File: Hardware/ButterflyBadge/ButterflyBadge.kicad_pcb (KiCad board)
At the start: 2 copper layers, 18 x 65 mm, 614 parts, among them J1 USB_C_Receptacle_USB2.0, M1 Motor_DC, P1 TC2030-CTX, Q1 ALS-PT19, SW1 SW_Push, SW3 SW_SPDT, U1 W25Q128JVS, U11 SN74LV1T34DBV, U12 SN74LV1T34DBV, U13 XC6206PxxxMR, U19 SN74LV1T34DBV, U2 CN3058, U20 SN74LV1T34DBV, U21 XC6206PxxxMR, U23 HX612, U25 AP3722AT, U3 RP2040, U4 AX5201, U5 AMS1117-3.3, U6 Si24R1, U7 TFDU4301, U8 SM351LT, U9 TMI8118, X1 Badgelife_sao_connector_v169b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, X2 Badgelife_sao_connector_v169b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, Y1 12MHz, Y2 16MHz

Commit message: More schematic and PCB work Bang
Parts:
- AE1, J1: moved to B.Cu
- BT1: footprint Battery:BatteryHolder_Keystone_1042_1x18650 -> Battery:BatteryHolder_Keystone_2460_1xAA; moved to B.Cu
- P1: footprint Resistor_SMD:R_0402_1005Metric -> Tag-Connect:TC2030-MCP-NL
- U4: footprint Package_SO:SOIC-8-1EP_3.9x4.9mm_P1.27mm_EP2.29x3mm_ThermalVias -> Package_SO:SOIC-8_3.9x4.9mm_P1.27mm
- moved R11 299.4 mm to (109.5, -104.0)
- moved R10 298.6 mm to (109.5, -105.0)
- moved R3 298.0 mm to (99.0, -79.5)
- moved P1 289.9 mm to (99.0, -82.0)
- moved R1 288.8 mm to (95.5, -71.5)
- moved C3 285.0 mm to (108.5, -69.4)
- moved C9 282.1 mm to (111.4, -73.3)
- moved C11 282.1 mm to (111.4, -69.4)
- moved SW1 281.4 mm to (89.0, -72.5)
- moved C10 280.9 mm to (111.4, -71.4)
- moved R17 280.0 mm to (155.0, -125.0), turned to 90 degrees
- moved R22 279.7 mm to (111.4, -65.5)
- moved C5 279.4 mm to (108.5, -65.5)
- moved R6 279.4 mm to (120.0, -83.0)
- moved R4 279.1 mm to (164.5, -127.0)
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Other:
- board size 18 x 65 mm -> 20 x 80.5 mm

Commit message: Hardware mods
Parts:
- removed AE1: Antenna, RF_Antenna:Texas_SWRA117D_2.4GHz_Left
- removed REF**: BatteryHolder_Keystone_2460_1xAA, Battery:BatteryHolder_Keystone_2460_1xAA
- added AE2: Antenna_Chip, Resistor_SMD:R_1206_3216Metric, F.Cu at (163.5, -83.8)
- C20: footprint Capacitor_SMD:C_0603_1608Metric -> Capacitor_SMD:C_0402_1005Metric
- moved C2 66.4 mm to (155.2, -103.0)
- moved Y1 66.4 mm to (155.2, -105.2)
- moved SW1 64.8 mm to (152.8, -84.2), turned to -90 degrees
- moved C4 62.7 mm to (156.5, -107.8), turned to 180 degrees
- moved R22 58.8 mm to (158.8, -100.2), turned to -90 degrees
- moved R1 58.6 mm to (151.2, -89.5)
- moved R3 57.7 mm to (152.0, -102.2), turned to 90 degrees
- moved C13 56.5 mm to (158.8, -98.2), turned to -90 degrees
- moved R7 55.3 mm to (158.8, -121.5), turned to -90 degrees
- moved P1 55.3 mm to (149.8, -104.0), turned to 90 degrees
- moved R6 53.9 mm to (157.8, -121.5), turned to -90 degrees
- moved C11 53.5 mm to (159.0, -93.8), turned to -90 degrees
- moved D518 52.3 mm to (158.0, -102.2), turned to 180 degrees
- moved C9 51.3 mm to (153.8, -102.2), turned to 90 degrees
- moved C5 50.5 mm to (151.8, -91.5), turned to 180 degrees
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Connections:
- net Net-(U3-USB_DM) renamed /USB_RES+
- net Net-(U3-USB_DP) renamed /USB_RES-
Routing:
- net unconnected-(AE2-PCB_Trace): track 0.00 -> 3.27 mm

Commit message: Almost had the PCB done, need to restart. Sad face
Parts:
- removed AE2: Antenna_Chip, Resistor_SMD:R_1206_3216Metric
- removed C35, C38: 22uF, Capacitor_SMD:C_1206_3216Metric
- removed C36, C39: 10uF, Capacitor_SMD:C_0603_1608Metric
- removed C37, C40: 1uF, Capacitor_SMD:C_0402_1005Metric
- removed D10, D100, D101, D102, D103, D104, D105, D106, D107, D108, D109, D11, D110, D111, D112, D113, D114, D115, D116, D117, D118, D119, D12, D120, D121, D122, D123, D124, D125, D126, D127, D128, D129, D13, D130, D131, D132, D133, D134, D135, D136, D137, D138, D139, D14, D140, D141, D142, D143, D144, D145, D146, D147, D148, D149, D15, D150, D151, D152, D153, D154, D155, D156, D157, D158, D159, D16, D160, D161, D162, D163, D164, D165, D166, D167, D168, D169, D17, D170, D171, D172, D173, D174, D175, D176, D177, D178, D179, D18, D180, D181, D182, D183, D184, D185, D186, D187, D188, D189, D19, D190, D191, D192, D193, D194, D195, D196, D197, D198, D199, D20, D200, D201, D202, D203, D204, D205, D206, D207, D208, D209, D21, D210, D211, D212, D213, D214, D215, D216, D217, D218, D219, D22, D220, D221, D222, D223, D224, D225, D226, D227, D228, D229, D23, D230, D231, D232, D233, D234, D235, D236, D237, D238, D239, D24, D240, D241, D242, D243, D244, D245, D246, D247, D248, D249, D25, D250, D251, D252, D253, D254, D255, D256, D257, D258, D259, D26, D260, D261, D262, D263, D264, D265, D266, D267, D268, D269, D27, D270, D271, D272, D273, D274, D275, D276, D277, D278, D279, D28, D280, D281, D282, D283, D284, D285, D286, D287, D288, D289, D29, D290, D291, D292, D293, D294, D295, D296, D297, D298, D299, D3, D30, D300, D301, D302, D303, D304, D305, D306, D307, D308, D309, D31, D310, D311, D312, D313, D314, D315, D316, D317, D318, D319, D32, D320, D321, D322, D323, D324, D325, D326, D327, D328, D329, D33, D330, D331, D332, D333, D334, D335, D336, D337, D338, D339, D34, D340, D341, D342, D343, D344, D345, D346, D347, D348, D349, D35, D350, D351, D352, D353, D354, D355, D356, D357, D358, D359, D36, D360, D361, D362, D363, D364, D365, D366, D367, D368, D369, D37, D370, D371, D372, D373, D374, D375, D376, D377, D378, D379, D38, D380, D381, D382, D383, D384, D385, D386, D387, D388, D389, D39, D390, D391, D392, D393, D394, D395, D396, D397, D398, D399, D4, D40, D400, D401, D402, D403, D404, D405, D406, D407, D408, D409, D41, D410, D411, D412, D413, D414, D415, D416, D417, D418, D419, D42, D420, D421, D422, D423, D424, D425, D426, D427, D428, D429, D43, D430, D431, D432, D433, D434, D435, D436, D437, D438, D439, D44, D440, D441, D442, D443, D444, D445, D446, D447, D448, D449, D45, D450, D451, D452, D453, D454, D455, D456, D457, D458, D459, D46, D460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: SK6812, XL3528RGBW:XL-3528RGBW
- removed U11, U12, U19, U20: SN74LV1T34DBV, Package_TO_SOT_SMD:SOT-23-5
- removed U13, U21: XC6206PxxxMR, Package_TO_SOT_SMD:SOT-23
- removed U16: ~, Package_SO:SOP-8_3.9x4.9mm_P1.27mm
- removed U23: HX612, Package_SO:SOP-16_3.9x9.9mm_P1.27mm
- removed X1, X2: Badgelife_sao_connector_v169bis, badgelife_sao_v169bis:Badgelife-SAOv169-BADGE-2x3
- added AE1: Antenna, RF_Antenna:Texas_SWRA117D_2.4GHz_Left, F.Cu at (40.8, 124.7)
- added BZ1: Buzzer, ButterflyBadge:Buzzer-GSC5025YA-12R4000, F.Cu at (38.6, 128.8)
- added J4: Conn_02x07_Odd_Even, ButterflyBadge:FlatFlexWingConnector-PCBSide, F.Cu at (30.2, 127.9)
- added Q2: Q_NMOS_GSD, Package_TO_SOT_SMD:SOT-23, F.Cu at (36.1, 134.2)
- added R23: 0, Resistor_SMD:R_0402_1005Metric, F.Cu at (40.0, 132.9)
- added R24: 10K, Resistor_SMD:R_0402_1005Metric, F.Cu at (40.0, 134.9)
- BT1: footprint Battery:BatteryHolder_Keystone_2460_1xAA -> Battery:BatteryHolder_MPD_BH-18650-PC2
- U4: footprint Package_SO:SOIC-8_3.9x4.9mm_P1.27mm -> Package_SO:SOIC-8-1EP_3.9x4.9mm_P1.27mm_EP2.41x3.3mm_ThermalVias
- moved C15 207.1 mm to (228.2, 81.0)
- moved C21 207.1 mm to (229.2, 89.3)
- moved C42 207.1 mm to (220.2, 84.0)
- moved C43 207.1 mm to (229.2, 86.3)
- moved D2 207.1 mm to (234.2, 89.8)
- moved L1 207.1 mm to (233.7, 95.3)
- moved R12 207.1 mm to (229.2, 85.3)
- moved R13 207.1 mm to (229.2, 84.3)
- moved R8 207.1 mm to (231.7, 81.3)
- moved R9 207.1 mm to (236.7, 80.3)
- moved U5 207.1 mm to (222.2, 78.8)
- moved C16 201.6 mm to (91.5, 125.5)
- moved SW3 201.2 mm to (197.8, 135.6)
- moved C29 198.9 mm to (122.0, 127.4)
- moved C30 198.9 mm to (118.5, 132.4)
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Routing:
- net unconnected-(AE2-PCB_Trace): track 3.27 -> 0.00 mm
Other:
- board size 20 x 80.5 mm -> 26.7 x 96.5 mm

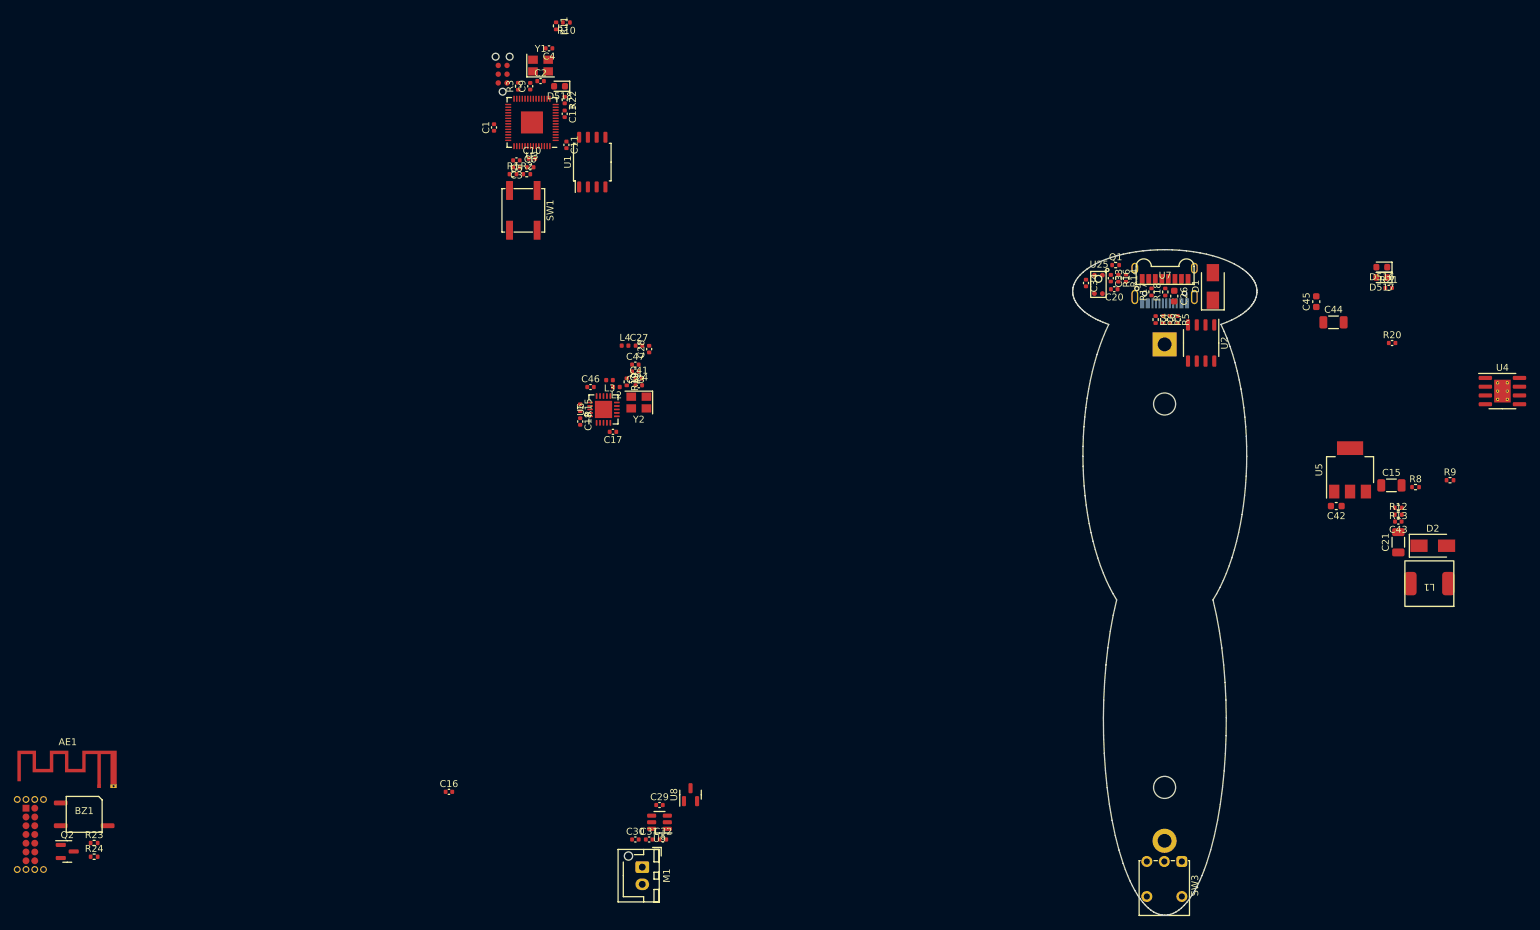
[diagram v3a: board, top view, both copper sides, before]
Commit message: Component placement is done, now for layout
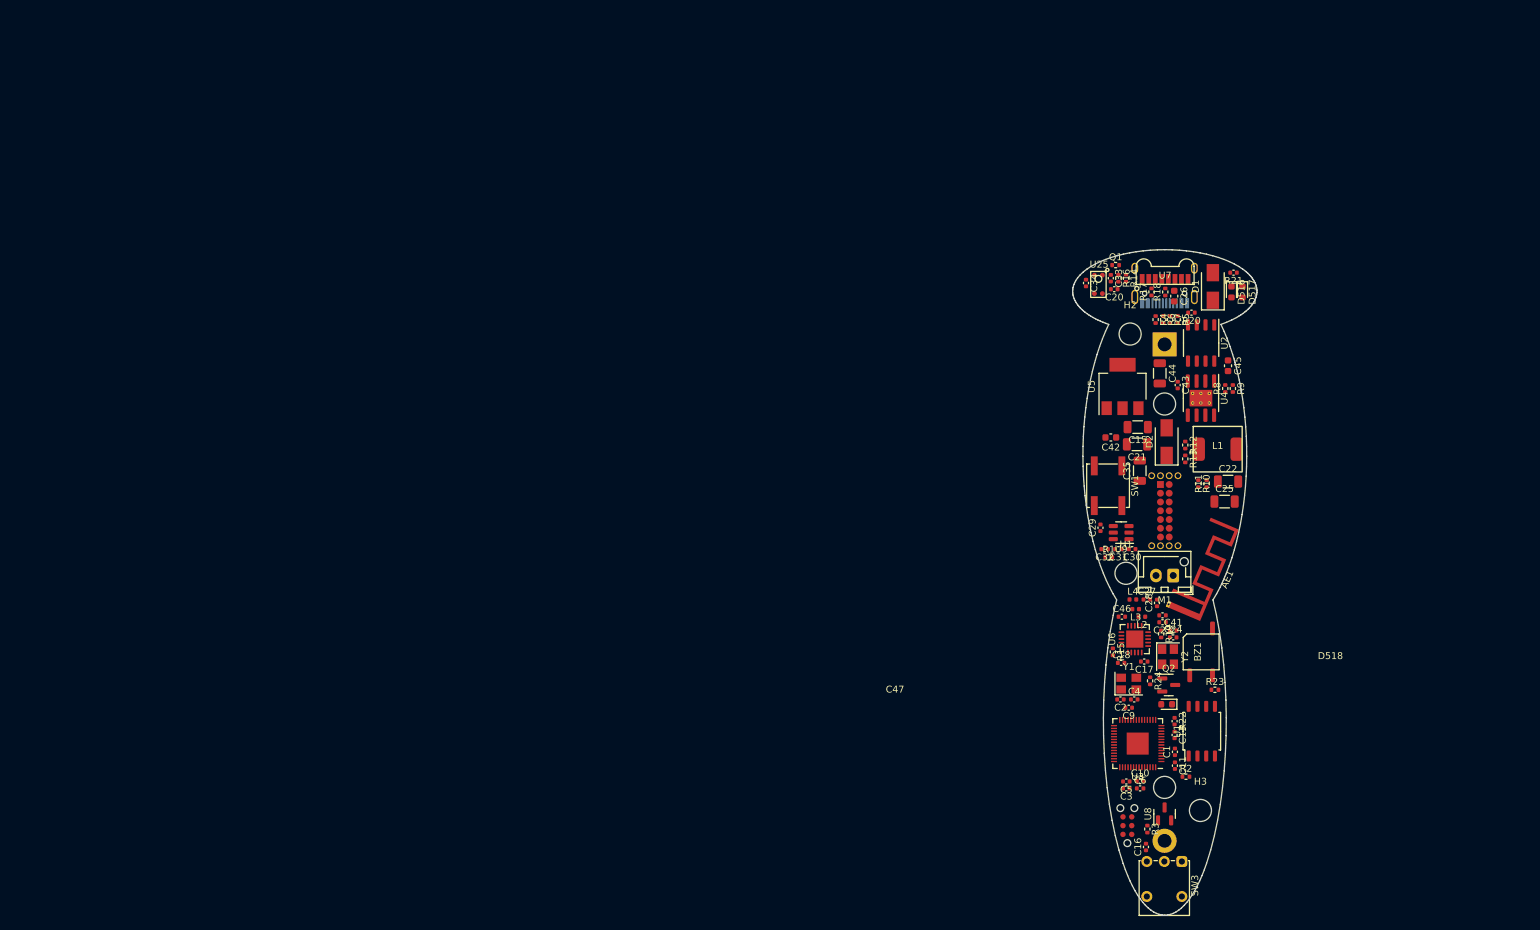
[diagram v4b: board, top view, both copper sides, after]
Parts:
- added C22: 22uF, Capacitor_SMD:C_1206_3216Metric, F.Cu at (204.5, 80.5)
- added C25: 22uF, Capacitor_SMD:C_1206_3216Metric, F.Cu at (204.0, 83.4)
- added C35: 22uF, Capacitor_SMD:C_1206_3216Metric, F.Cu at (191.7, 78.9)
- added H1: , MountingHole:MountingHole_3.2mm_M3, F.Cu at (189.7, 93.8)
- added H2: , MountingHole:MountingHole_3.2mm_M3, F.Cu at (190.3, 59.1)
- added H3: , MountingHole:MountingHole_3.2mm_M3, F.Cu at (200.5, 128.2)
- moved J4 171.1 mm to (194.7, 80.9)
- moved R23 164.1 mm to (202.6, 110.7)
- moved BZ1 163.7 mm to (200.6, 105.2), turned to 90 degrees
- moved Q2 161.6 mm to (195.9, 110.0)
- moved AE1 158.5 mm to (196.7, 96.4), turned to -113 degrees
- moved R24 155.3 mm to (193.2, 109.4), turned to -90 degrees
- moved P1 141.7 mm to (189.9, 130.4)
- moved R3 141.2 mm to (192.8, 130.9), turned to -90 degrees
- moved C1 134.0 mm to (196.8, 119.7)
- moved R2 129.5 mm to (198.4, 123.3)
- moved C4 127.0 mm to (190.9, 112.1), turned to 0 degrees
- moved C13 126.3 mm to (196.8, 117.2)
- moved C3 126.3 mm to (189.8, 125.0)
- moved C5 126.3 mm to (189.8, 124.0)
- moved C6 126.3 mm to (191.8, 125.0)
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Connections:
- C30 pad 2: Net-(M1-+) -> Net-(U9-OUTB)
- C31 pad 1: Net-(M1-+) -> Net-(U9-OUTB)
- C31 pad 2: Net-(M1--) -> Net-(U9-OUTA)
- C32 pad 1: Net-(M1--) -> Net-(U9-OUTA)
- M1 pad 1: Net-(M1-+) -> unconnected-(M1-+)
- M1 pad 2: Net-(M1--) -> unconnected-(M1--)
- Q2 pad 1: Net-(Q2-G) -> /BUZZER
- R24 pad 1: Net-(Q2-G) -> /BUZZER
- U3 pad 29: unconnected-(U3-GPIO18) -> /BUZZER
- U9 pad 1: Net-(M1-+) -> Net-(U9-OUTB)
- U9 pad 6: Net-(M1--) -> Net-(U9-OUTA)

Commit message: Commit before I try to ripup everything on a whim
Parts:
- moved R23 30.6 mm to (191.1, 82.4), turned to -90 degrees
- moved R24 23.6 mm to (198.0, 132.5)
- moved C9 13.2 mm to (192.5, 126.2), turned to -90 degrees
- moved Q2 13.1 mm to (199.0, 122.8), turned to 90 degrees
- moved C13 8.94 mm to (200.8, 109.2), turned to 0 degrees
- moved R22 5.55 mm to (196.7, 109.7), turned to 0 degrees
- moved C11 5.49 mm to (202.2, 121.0)
- moved R2 5.37 mm to (203.2, 121.0), turned to 90 degrees
- moved C1 4.64 mm to (201.2, 121.0), turned to -90 degrees
- moved D518 3.89 mm to (194.0, 109.2)
- moved C4 2.37 mm to (188.6, 111.6), turned to 180 degrees
- moved C10 2.37 mm to (191.0, 126.2)
- moved C3 2.37 mm to (189.0, 127.2)
- moved C5 2.37 mm to (189.0, 126.2)
- moved C6 2.37 mm to (191.0, 127.2)
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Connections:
- U3 pad 16: /HALL_SENSOR -> /STBD_LED_1
- U3 pad 29: /BUZZER -> /SCK
- U3 pad 30: /PORT_LED_2 -> /COPI
- U3 pad 31: /PORT_LED_1 -> /CIPO
- U3 pad 32: /STBD_LED_1 -> /NRF_CS
- U3 pad 34: unconnected-(U3-GPIO22) -> /NRF_CE
- U3 pad 35: /MOTOR_A -> /NRF_IRQ
- U3 pad 4: /SCK -> unconnected-(U3-GPIO2)
- U3 pad 41: unconnected-(U3-GPIO29_ADC3) -> /HALL_SENSOR
- U3 pad 5: /COPI -> unconnected-(U3-GPIO3)
- U3 pad 6: /CIPO -> unconnected-(U3-GPIO4)
- U3 pad 7: /NRF_CS -> unconnected-(U3-GPIO5)
- U3 pad 8: /NRF_CE -> unconnected-(U3-GPIO6)
- U3 pad 9: /NRF_IRQ -> unconnected-(U3-GPIO7)
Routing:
- net /AMBIENT_LIGHT: track 0.00 -> 54.1 mm, vias 0 -> 2
- net /MIC_OUT: track 0.00 -> 48.8 mm, vias 0 -> 2
- net Net-(U3-GPIO27_ADC1): track 0.00 -> 40.0 mm, vias 0 -> 2
- net /USB_RES-: track 0.00 -> 30.2 mm, vias 0 -> 2
- net Net-(BZ1-+): track 0.00 -> 26.0 mm, vias 0 -> 2
- net /NRF_IRQ: track 0.00 -> 21.4 mm, vias 0 -> 2
- net Net-(U1-DI(IO0)): track 0.00 -> 17.8 mm, vias 0 -> 2
- net +3V3: track 0.00 -> 17.7 mm, vias 0 -> 2
- net Net-(U1-CLK): track 0.00 -> 17.1 mm, vias 0 -> 2
- net /NRF_CE: track 0.00 -> 15.7 mm, vias 0 -> 2
- net Net-(U1-IO3): track 0.00 -> 15.5 mm, vias 0 -> 2
- net Net-(U1-IO2): track 0.00 -> 15.2 mm, vias 0 -> 2
- net /CIPO: track 0.00 -> 14.1 mm, vias 0 -> 2
- net /STBD_LED_2: track 0.00 -> 13.7 mm, vias 0 -> 1
- net /SDA: track 0.00 -> 13.6 mm, vias 0 -> 1
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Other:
- copper layers 2 -> 4

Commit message: More routing
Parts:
- removed C3: 0.1uF, Capacitor_SMD:C_0402_1005Metric
- added TP1: , TestPoint:TestPoint_Pad_D1.0mm, F.Cu at (194.6, 75.2)
- added TP2: , TestPoint:TestPoint_Pad_D1.0mm, F.Cu at (196.7, 75.2)
- added TP3: , TestPoint:TestPoint_Pad_D1.0mm, F.Cu at (197.7, 69.9)
- moved R21 79.8 mm to (189.8, 128.5)
- moved P1 77.8 mm to (203.9, 55.2), turned to 180 degrees
- moved R24 75.4 mm to (188.2, 57.7)
- moved D516 74.9 mm to (189.1, 126.2), turned to 90 degrees
- moved D517 74.9 mm to (190.7, 126.2), turned to 90 degrees
- moved BT1 71.4 mm to (195.3, 132.0), turned to 90 degrees
- moved C44 68.3 mm to (190.5, 133.0)
- moved Q2 66.4 mm to (191.1, 56.8)
- moved C43 62.8 mm to (202.2, 129.1)
- moved R8 62.4 mm to (197.8, 129.1)
- moved R9 62.4 mm to (198.9, 129.1)
- moved C45 61.7 mm to (188.9, 123.4), turned to 0 degrees
- moved U2 59.3 mm to (189.8, 118.7)
- moved R20 58.8 mm to (189.9, 114.1)
- moved D1 58.8 mm to (190.3, 109.8), turned to 180 degrees
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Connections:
- net Net-(D1-K) renamed /5V_UNSWITCHED
- D518 pad 2: Net-(D518-A) -> /LED
- M1 pad 1: unconnected-(M1-+) -> Net-(U9-OUTB)
- M1 pad 2: unconnected-(M1--) -> Net-(U9-OUTA)
- U3 pad 11: /IRDA_SD -> /CIPO
- U3 pad 12: /STBD_GP1 -> /NRF_IRQ
- U3 pad 13: /STBD_GP0 -> /MOTOR_B
- U3 pad 14: /PORT_GP1 -> /MOTOR_A
- U3 pad 15: /PORT_GP0 -> /STBD_GP1
- U3 pad 16: /STBD_LED_1 -> /PORT_GP1
- U3 pad 17: Net-(D518-A) -> /STBD_GP0
- U3 pad 18: /STBD_LED_2 -> /PORT_GP0
- U3 pad 29: /SCK -> /STBD_LED_2
- U3 pad 30: /COPI -> /PORT_LED_2
- U3 pad 31: /CIPO -> /STBD_LED_1
- U3 pad 32: /NRF_CS -> /PORT_LED_1
- U3 pad 34: /NRF_CE -> /LED
- U3 pad 35: /NRF_IRQ -> Net-(U3-GPIO23)
- U3 pad 36: /MOTOR_B -> Net-(U3-GPIO24)
- U3 pad 37: /MOTOR_A -> Net-(U3-GPIO25)
- U3 pad 38: /MIC_OUT -> /BUZZER
- U3 pad 4: unconnected-(U3-GPIO2) -> /IRDA_SD
- U3 pad 41: /HALL_SENSOR -> /MIC_OUT
- U3 pad 5: unconnected-(U3-GPIO3) -> /HALL_SENSOR
- U3 pad 6: unconnected-(U3-GPIO4) -> /NRF_CE
- U3 pad 7: unconnected-(U3-GPIO5) -> /NRF_CS
- U3 pad 8: unconnected-(U3-GPIO6) -> /SCK
- U3 pad 9: unconnected-(U3-GPIO7) -> /COPI
- U6 pad 21: (no net) -> GND
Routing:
- net GND: track 7.80 -> 131.5 mm, vias 0 -> 23
- net +3V3: track 17.7 -> 125.4 mm, vias 2 -> 12
- net /VUSB: track 0.00 -> 104.5 mm, vias 0 -> 4
- net +5V: track 0.00 -> 92.6 mm, vias 0 -> 5
- net /BATTERY_RAW: track 0.00 -> 90.6 mm, vias 0 -> 5
- net /HALL_SENSOR: track 0.88 -> 65.9 mm, vias 0 -> 2
- net /AMBIENT_LIGHT: track 54.1 -> 0.00 mm, vias 2 -> 0
- net /MIC_OUT: track 48.8 -> 0.00 mm, vias 2 -> 0
- net /5V_UNSWITCHED: track 0.00 -> 46.0 mm, vias 0 -> 2
- net /IRDA_SD: track 0.00 -> 33.9 mm, vias 0 -> 2
- net Net-(U3-GPIO27_ADC1): track 40.0 -> 6.34 mm, vias 2 -> 0
- net /IRDA_RX: track 0.00 -> 31.1 mm, vias 0 -> 2
- net /CIPO: track 14.1 -> 42.8 mm
- net /IRDA_TX: track 0.00 -> 28.4 mm, vias 0 -> 2
- net /SCK: track 11.3 -> 38.5 mm
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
